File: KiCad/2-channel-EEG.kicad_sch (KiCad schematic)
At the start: 32 parts, among them J1 Power Input, J2 CH1, SW1 SW_Push_SPDT, U1 PDME2-5-D5-D, U2 AD8237, U3 AD8606, U4 AD8606, U5 TCR2EF33, U6 AD8606

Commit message: fixed power connections on U3A, added output filter
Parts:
- removed C9: 0.1u, symbol Device:C_Small
- added C10, C11: 100n, symbol Device:C_Small
- added C7: 0.1u, symbol Device:C_Small
- added R10, R14: 56k, symbol Device:R_US
- renumbered C10 to C12, C7 to C8, C8 to C9, R10 to R11, R11 to R12, R12 to R13
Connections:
- net +3.3V: now also C7.2
- net GND: now also C7.1
- net VGND: now also U3.3 (+), C11.1; no longer U3.5 (+), U6.5 (+)
- net at C6.1, U2.6 (VREF): now also U3.1; no longer U3.7
- net at R3.1, R5.2, U2.8: now also U3.5 (+); no longer U3.3 (+)
- net at C6.2, R5.1: now also U3.2 (-); no longer U3.6 (-)
- net at R7.2, R8.1: now also U3.6 (-); no longer U3.2 (-)
- net at R8.2: now also U3.7, R10.2; no longer U3.1
- net at U6.6 (-), U6.7: now also C10.2
- new net: C11.2, R14.1, U6.5 (+)
- new net: C10.1, R10.1, R14.2
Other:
- note removed: "Termination of unused opamp"
- note removed: "To Do: Filters"
- moved on the sheet: C5, C6, C8, R1, R11, R2, R6, R9, U4A, U4B, U6B

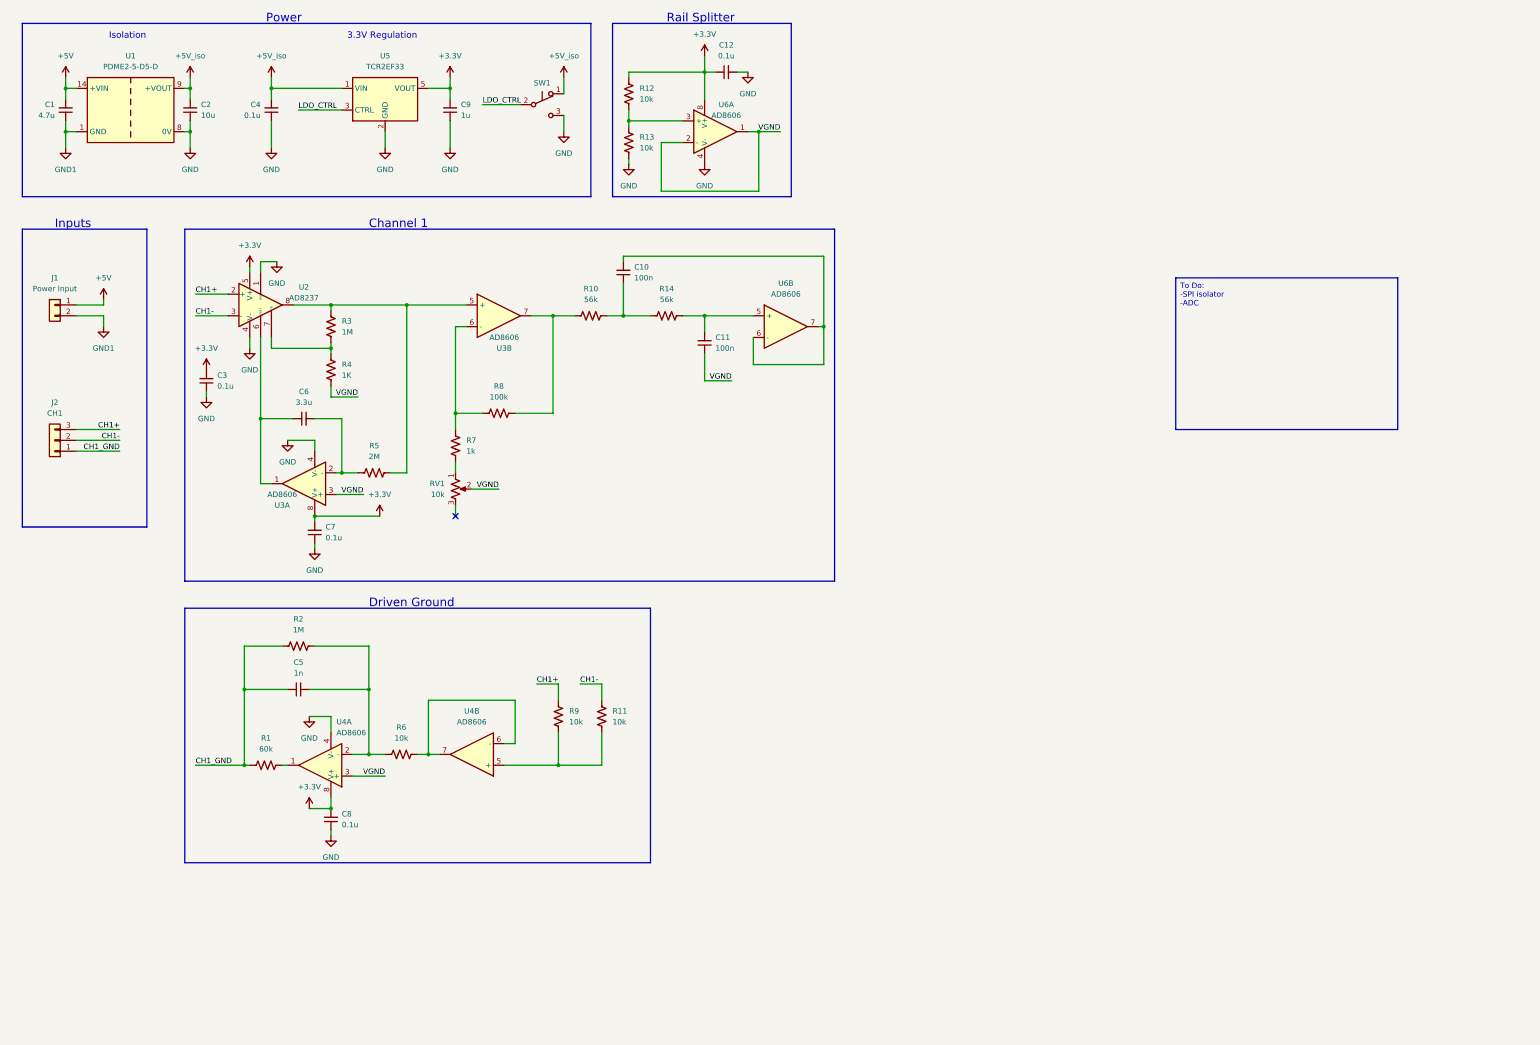
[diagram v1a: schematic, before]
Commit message: add 2nd channel, start pcb
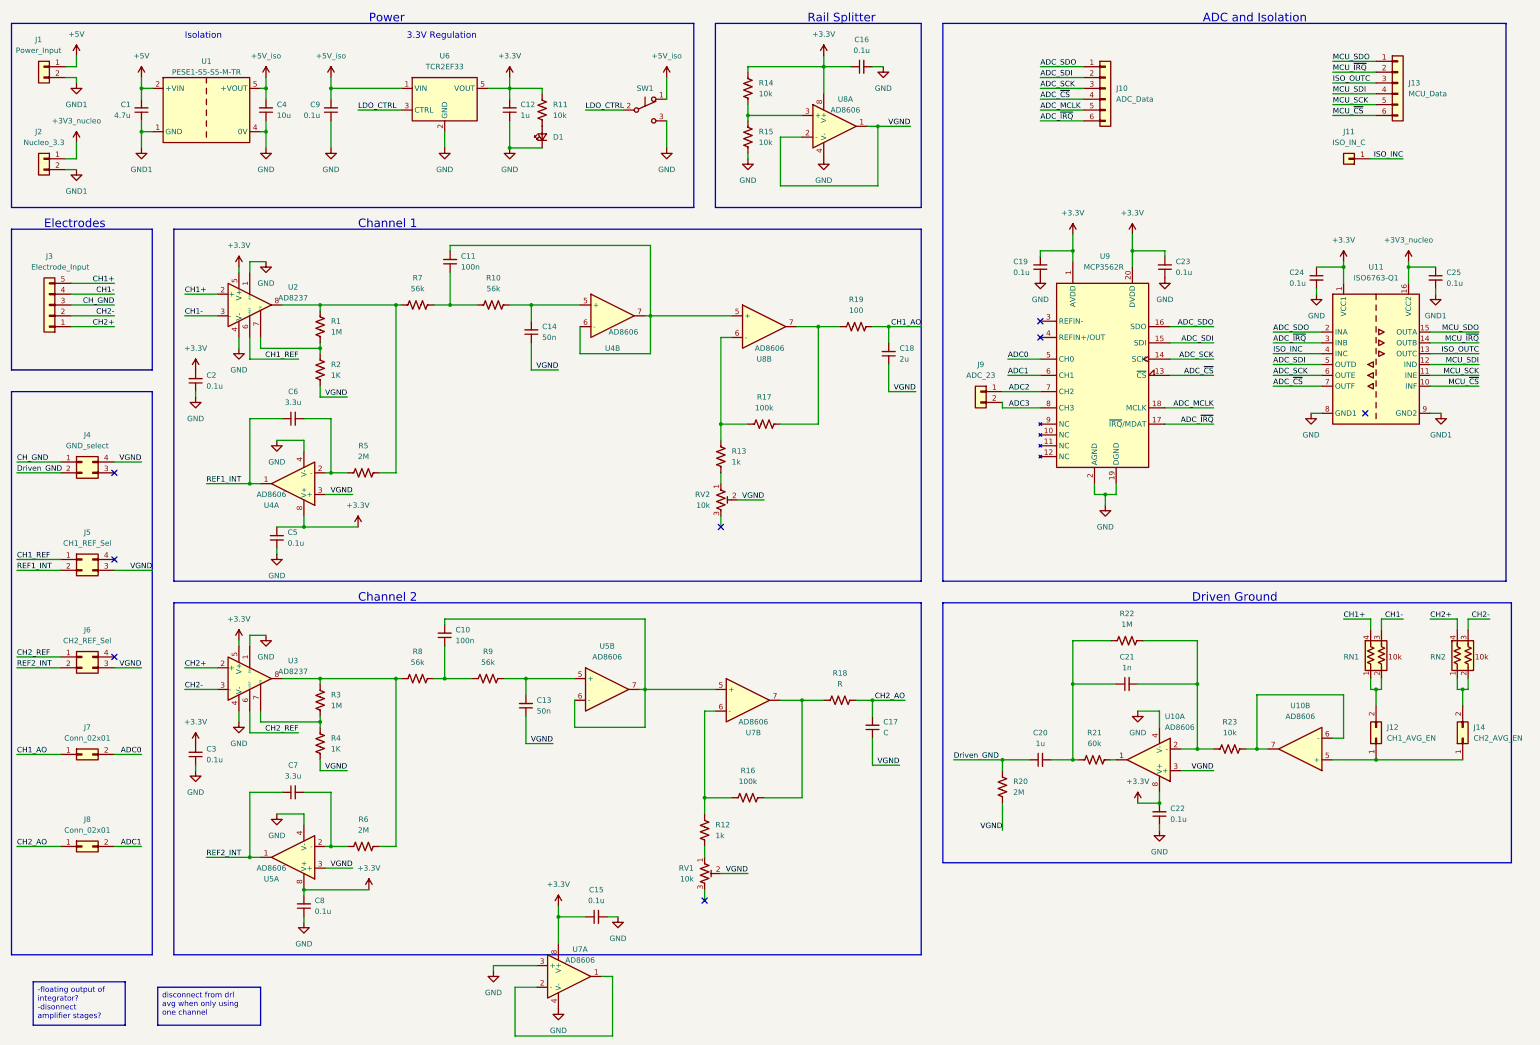
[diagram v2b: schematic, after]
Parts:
- removed J2: CH1, symbol Connector_Generic:Conn_01x03
- removed R14: 56k, symbol Device:R_US
- removed RV1: 10k, symbol Device:R_Potentiometer_US
- removed U1: PDME2-5-D5-D, symbol Senior_Project_Library:PDME2-5-D5-D
- removed U3: AD8606, symbol Senior_Project_Library:AD8606
- removed unit 2 of U6
- added C13, C14: 50n, Capacitor_SMD:C_0805_2012Metric_Pad1.18x1.45mm_HandSolder, symbol Device:C_Small
- added C15, C19, C23, C24, C25, C3, C5, C8: 0.1u, Capacitor_SMD:C_0805_2012Metric_Pad1.18x1.45mm_HandSolder, symbol Device:C_Small
- added C17: C, Capacitor_SMD:C_0805_2012Metric_Pad1.18x1.45mm_HandSolder, symbol Device:C_Small
- added C18: 2u, Capacitor_SMD:C_0805_2012Metric_Pad1.18x1.45mm_HandSolder, symbol Device:C_Small
- added C20: 1u, Capacitor_SMD:C_0805_2012Metric_Pad1.18x1.45mm_HandSolder, symbol Device:C_Small
- added D1: ~, LED_SMD:LED_0603_1608Metric_Pad1.05x0.95mm_HandSolder, symbol Device:LED_Small
- added J10: ADC_Data, Connector_PinHeader_2.54mm:PinHeader_1x06_P2.54mm_Vertical, symbol Connector_Generic:Conn_01x06
- added J11: ISO_IN_C, Connector_PinHeader_2.54mm:PinHeader_1x01_P2.54mm_Vertical, symbol Connector_Generic:Conn_01x01
- added J12: CH1_AVG_EN, Connector_PinHeader_2.54mm:PinHeader_2x01_P2.54mm_Vertical, symbol Connector_Generic:Conn_02x01
- added J13: MCU_Data, Connector_PinHeader_2.54mm:PinHeader_1x06_P2.54mm_Vertical, symbol Connector_Generic:Conn_01x06
- added J14: CH2_AVG_EN, Connector_PinHeader_2.54mm:PinHeader_2x01_P2.54mm_Vertical, symbol Connector_Generic:Conn_02x01
- added J2: Nucleo_3.3, Connector_PinHeader_2.54mm:PinHeader_1x02_P2.54mm_Vertical, symbol Connector_Generic:Conn_01x02
- added J3: Electrode_Input, Connector_PinHeader_2.54mm:PinHeader_1x05_P2.54mm_Vertical, symbol Connector_Generic:Conn_01x05
- added J4: GND_select, Connector_PinHeader_2.54mm:PinHeader_2x02_P2.54mm_Vertical, symbol Connector_Generic:Conn_02x02_Counter_Clockwise
- added J5: CH1_REF_Sel, Connector_PinHeader_2.54mm:PinHeader_2x02_P2.54mm_Vertical, symbol Connector_Generic:Conn_02x02_Counter_Clockwise
- added J6: CH2_REF_Sel, Connector_PinHeader_2.54mm:PinHeader_2x02_P2.54mm_Vertical, symbol Connector_Generic:Conn_02x02_Counter_Clockwise
- added J7, J8: Conn_02x01, Connector_PinHeader_2.54mm:PinHeader_2x01_P2.54mm_Vertical, symbol Connector_Generic:Conn_02x01
- added J9: ADC_23, Connector_PinHeader_2.54mm:PinHeader_2x01_P2.54mm_Vertical, symbol Connector_Generic:Conn_01x02
- added R12, R13: 1k, Resistor_SMD:R_0805_2012Metric_Pad1.20x1.40mm_HandSolder, symbol Device:R_US
- added R16, R17: 100k, Resistor_SMD:R_0805_2012Metric_Pad1.20x1.40mm_HandSolder, symbol Device:R_US
- added R18: R, Resistor_SMD:R_0805_2012Metric_Pad1.20x1.40mm_HandSolder, symbol Device:R_US
- added R19: 100, Resistor_SMD:R_0805_2012Metric_Pad1.20x1.40mm_HandSolder, symbol Device:R_US
- added R20, R6: 2M, Resistor_SMD:R_0805_2012Metric_Pad1.20x1.40mm_HandSolder, symbol Device:R_US
- added R3: 1M, Resistor_SMD:R_0805_2012Metric_Pad1.20x1.40mm_HandSolder, symbol Device:R_US
- added R4: 1K, Resistor_SMD:R_0805_2012Metric_Pad1.20x1.40mm_HandSolder, symbol Device:R_US
- added RN1, RN2: Matched_10K_Resistor_Array_2x, Senior_Project_Footprints:R_Array_Matched_2x0606, symbol Senior_Project_Library:Matched_10K_Resistor_Array_2x
- added RV1, RV2: 10k, Senior_Project_Footprints:TRIM_35WR10KLFTR, symbol Senior_Project_Library:R_Potentiometer_35WR10KLFTR_10K
- added U1: PESE1-S5-S5-M-TR, Senior_Project_Footprints:CONV_PESE1-S5-S5-M, symbol Senior_Project_Library:PESE1-S5-S5-M-TR
- added U11: ISO6763-Q1, Package_SO:SOIC-16W_7.5x10.3mm_P1.27mm, symbol Senior_Project_Library:ISO6763-Q1
- added U3: AD8237, Package_SO:MSOP-8_3x3mm_P0.65mm, symbol Senior_Project_Library:AD8237
- added U4, U5, U7: AD8606, Package_SO:MSOP-8_3x3mm_P0.65mm, symbol Senior_Project_Library:AD8606
- added unit 2 of U8
- added U9: MCP3562R, Package_QFP:TQFP-52-1EP_10x10mm_P0.65mm_EP6.5x6.5mm, symbol Senior_Project_Library:MCP3562R
- C1, C10, C11, C6: footprint (none) -> Capacitor_SMD:C_0805_2012Metric_Pad1.18x1.45mm_HandSolder
- C12: renamed from C9; footprint (none) -> Capacitor_SMD:C_0805_2012Metric_Pad1.18x1.45mm_HandSolder
- C16: renamed from C12; footprint (none) -> Capacitor_SMD:C_0805_2012Metric_Pad1.18x1.45mm_HandSolder
- C2: renamed from C3; footprint (none) -> Capacitor_SMD:C_0805_2012Metric_Pad1.18x1.45mm_HandSolder
- C21: renamed from C5; footprint (none) -> Capacitor_SMD:C_0805_2012Metric_Pad1.18x1.45mm_HandSolder
- C22: renamed from C8; footprint (none) -> Capacitor_SMD:C_0805_2012Metric_Pad1.18x1.45mm_HandSolder
- C4: renamed from C2; footprint (none) -> Capacitor_SMD:C_0805_2012Metric_Pad1.18x1.45mm_HandSolder
- C7: value 0.1u -> 3.3u; footprint (none) -> Capacitor_SMD:C_0805_2012Metric_Pad1.18x1.45mm_HandSolder
- C9: renamed from C4; footprint (none) -> Capacitor_SMD:C_0805_2012Metric_Pad1.18x1.45mm_HandSolder
- J1: value Power Input -> Power_Input; footprint (none) -> Connector_PinHeader_2.54mm:PinHeader_1x02_P2.54mm_Vertical
- R1: renamed from R3; footprint (none) -> Resistor_SMD:R_0805_2012Metric_Pad1.20x1.40mm_HandSolder
- R10, R11, R5: footprint (none) -> Resistor_SMD:R_0805_2012Metric_Pad1.20x1.40mm_HandSolder
- R14: renamed from R12; footprint (none) -> Resistor_SMD:R_0805_2012Metric_Pad1.20x1.40mm_HandSolder
- R15: renamed from R13; footprint (none) -> Resistor_SMD:R_0805_2012Metric_Pad1.20x1.40mm_HandSolder
- R2: renamed from R4; footprint (none) -> Resistor_SMD:R_0805_2012Metric_Pad1.20x1.40mm_HandSolder
- R21: renamed from R1; footprint (none) -> Resistor_SMD:R_0805_2012Metric_Pad1.20x1.40mm_HandSolder
- R22: renamed from R2; footprint (none) -> Resistor_SMD:R_0805_2012Metric_Pad1.20x1.40mm_HandSolder
- R23: renamed from R6; footprint (none) -> Resistor_SMD:R_0805_2012Metric_Pad1.20x1.40mm_HandSolder
- R7: value 1k -> 56k; footprint (none) -> Resistor_SMD:R_0805_2012Metric_Pad1.20x1.40mm_HandSolder
- R8: value 100k -> 56k; footprint (none) -> Resistor_SMD:R_0805_2012Metric_Pad1.20x1.40mm_HandSolder
- R9: value 10k -> 56k; footprint (none) -> Resistor_SMD:R_0805_2012Metric_Pad1.20x1.40mm_HandSolder
- SW1: footprint (none) -> Senior_Project_Footprints:SW_JS102011SCQN
- U10: renamed from U4; footprint (none) -> Package_SO:MSOP-8_3x3mm_P0.65mm
- U2: footprint (none) -> Package_SO:MSOP-8_3x3mm_P0.65mm
- U6: renamed from U5; footprint Package_TO_SOT_SMD:SOT-553 -> Senior_Project_Footprints:IC_TC4S584F_LF
- U8: renamed from U6; footprint (none) -> Package_SO:MSOP-8_3x3mm_P0.65mm
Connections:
- net +3.3V: now also R11.2, C15.1, C19.2, C23.2, C24.1, C25.1, C3.2, C5.2, C8.2, J2.1 (Pin_1), U1.5 (+VOUT), U11.1 (VCC1), U11.16 (VCC2), U3.5 (V+), U4.8 (V+), U5.8 (V+), U7.8 (V+), U9.1 (AVDD), U9.20 (DVDD); no longer C7.2
- net +5V: now also U1.2 (+VIN)
- net CH1+: now also J3.5 (Pin_5), RN1.4; no longer R9.2
- net CH1-: now also J3.4 (Pin_4), RN1.3; no longer R11.2
- net GND: now also C15.2, C19.1, C23.1, C24.2, C3.1, C5.1, C8.1, D1.1 (K), U1.4 (0V), U11.8 (GND1), U3.1 (BW), U3.4 (V-), U4.4 (V-), U5.4 (V-), U7.3 (+), U7.4 (V-), U9.19 (DGND), U9.2 (AGND); no longer C7.1
- net GND1: now also C25.2, J2.2 (Pin_2), U1.1 (GND), U11.9 (GND2)
- net VGND: now also C13.1, C14.1, C17.1, C18.1, J4.4 (Pin_4), J5.3 (Pin_3), J6.3 (Pin_3), R20.1, R4.2, RV1.2, RV2.2, U4.3 (+), U5.3 (+); no longer C11.1
- net at R1.1, R5.2, U2.8: now also R7.2
- net at R8.1: now also C10.1, R9.2; no longer R7.2
- net at R10.2: now also C11.1, R7.1; no longer R8.2
- net CH1_REF: now reaches U2.6 (VREF)
- net CH1_REF: now also J5.1 (Pin_1); no longer C6.1
- net at C6.2, R5.1: now also U4.2 (-)
- net at C11.2: now also U4.6 (-), U4.7, U8.5 (+)
- net at R10.1: now also C14.2, U4.5 (+); no longer C10.1
- net at C10.2: now also U5.6 (-), U5.7, U7.5 (+)
- net CH1_GND: no longer names the net of C21.1, R21.1, R22.1
- net CH1_GND: now also C20.2
- new net: R13.1, RV2.1
- new net: U7.1, U7.2 (-)
- new net: R17.2, R19.2, U8.7
- new net: D1.2 (A), R11.1
- new net: R3.2, R4.1, U3.7 (FB)
- new net: C7.2, R6.1, U5.2 (-)
- new net: R3.1, R6.2, R8.2, U3.8
- new net: C13.2, R9.1, U5.5 (+)
- new net: J12.1 (Pin_1), J14.1 (Pin_1), U10.5 (+)
- new net: J14.2 (Pin_2), RN2.1, RN2.2
- new net: R12.2, R16.1, U7.6 (-)
- new net: R16.2, R18.2, U7.7
- new net: R13.2, R17.1, U8.6 (-)
- new net: R12.1, RV1.1
- new net: J12.2 (Pin_2), RN1.1, RN1.2
- new net ADC0: J7.2 (Pin_2), U9.5 (CH0)
- new net ADC1: J8.2 (Pin_2), U9.6 (CH1)
- new net ADC2: J9.1 (Pin_1), U9.7 (CH2)
- new net ADC3: J9.2 (Pin_2), U9.8 (CH3)
- new net ADC_MCLK: J10.5 (Pin_5), U9.18 (MCLK)
- new net ADC_SCK: J10.3 (Pin_3), U11.6 (OUTE), U9.14 (SCK)
- new net ADC_SDI: J10.2 (Pin_2), U11.5 (OUTD), U9.15 (SDI)
- new net ADC_SDO: J10.1 (Pin_1), U11.2 (INA), U9.16 (SDO)
- new net ADC_~{CS}: J10.4 (Pin_4), U11.7 (OUTF), U9.13 (~{CS})
- new net ADC_~{IRQ}: J10.6 (Pin_6), U11.3 (INB), U9.17 (~{IRQ}/MDAT)
- new net CH1_AO: C18.2, J7.1 (Pin_1), R19.1
- new net CH2+: J3.1 (Pin_1), RN2.4, U3.2 (+)
- new net CH2-: J3.2 (Pin_2), RN2.3, U3.3 (-)
- new net CH2_AO: C17.2, J8.1 (Pin_1), R18.1
- new net CH2_REF: J6.1 (Pin_1), U3.6 (VREF)
- new net CH_GND: J3.3 (Pin_3), J4.1 (Pin_1)
- new net Driven_GND: C20.1, J4.2 (Pin_2), R20.2
- new net ISO_INC: J11.1 (Pin_1), U11.4 (INC)
- new net ISO_OUTC: J13.3 (Pin_3), U11.13 (OUTC)
- new net MCU_SCK: J13.5 (Pin_5), U11.11 (INE)
- new net MCU_SDI: J13.4 (Pin_4), U11.12 (IND)
- new net MCU_SDO: J13.1 (Pin_1), U11.15 (OUTA)
- new net MCU_~{CS}: J13.6 (Pin_6), U11.10 (INF)
- new net MCU_~{IRQ}: J13.2 (Pin_2), U11.14 (OUTB)
- new net REF1_INT: C6.1, J5.2 (Pin_2), U4.1
- new net REF2_INT: C7.1, J6.2 (Pin_2), U5.1
- no-connect marks 1 -> 8
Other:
- note added: "ADC and Isolation"
- note added: "Channel 2"
- note added: "Electrodes"
- note removed: "Inputs"
- title: (none) -> 2-Channel EEG AFE
- moved on the sheet: C1, C12, C16, C2, C21, C22, C4, C6, C9, R1, R14, R15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
